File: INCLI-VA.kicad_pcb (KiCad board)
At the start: 2 copper layers, 100 x 70 mm, 186 parts, among them J1 MSTBV 2,5/5-GF-5,08, J2 MSTBV 2,5/2-GF-5,08, J401 USB4105-GF-A, J402 UART0, Q101 STD18NF25, Q102 IPD30N10S3L-34, Q701 DMN10H220LQ, Q702 BC817-40, Q703 BC807-40, Q751 DMN10H220LQ, Q752 BC817-40, Q753 BC807-40, SW401 RESET, SW402 BOOT, U101 LM74930QRGERQ1, U201 LMR38010SQDDARQ1, U301 TPS62A02QDRLRQ1, U302 LP5907QMFX-3.3Q1, U401 ESP32-S3-WROOM-1-N8R2, U402 USBLC6-2SC6, U501 SCL3300-D01, U502 ASM330LHHTR, U503 AS5147U-HTSM, U601 ADM3055E, U701 74AHCT1G126, U751 74AHCT1G126, U801 TPS3828-33Q1

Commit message: [Claude Code] PCB: adopta la propuesta 100x100 como INCLI-VA.kicad_pcb
Copia docs/layout/INCLI-VA-100x100.kicad_pcb sobre el PCB principal (sin
cambios propios desde 17a9676) y borra la copia duplicada de docs/layout.
DRC: 0 errores, 1 aviso U401, 396 sin rutear. Paridad: 22 diferencias por el
latch retirado; Update PCB from Schematic pendiente.

Co-Authored-By: Claude Opus 5.5 <noreply@anthropic.com>
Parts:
- removed H5: MountingHole_M3, MountingHole:MountingHole_3.2mm_M3
- TP101, TP102, TP103, TP104, TP201, TP301, TP302, TP303, TP304, TP305, TP501, TP502, TP503, TP504: moved to B.Cu
- moved H3 165.1 mm to (105.0, 145.0)
- moved SW401 163.0 mm to (181.0, 55.0)
- moved D601 152.8 mm to (116.0, 104.0)
- moved R754 151.9 mm to (195.0, 81.0), turned to 0 degrees
- moved R301 150.0 mm to (161.0, 118.0), turned to 0 degrees
- moved R752 149.7 mm to (190.5, 81.0)
- moved D752 149.5 mm to (193.5, 72.5), turned to 0 degrees
- moved C302 146.0 mm to (147.0, 120.0), turned to 0 degrees
- moved R755 145.9 mm to (196.0, 77.5), turned to 90 degrees
- moved R756 145.2 mm to (191.0, 84.0)
- moved SW402 145.0 mm to (186.0, 89.0)
- moved TP305 144.9 mm to (158.5, 138.5), turned to 180 degrees
- moved R108 144.5 mm to (115.0, 64.0)
- moved R112 144.5 mm to (144.0, 53.0)
- moved R603 144.2 mm to (116.0, 111.0)
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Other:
- board size 100 x 70 mm -> 100 x 100 mm

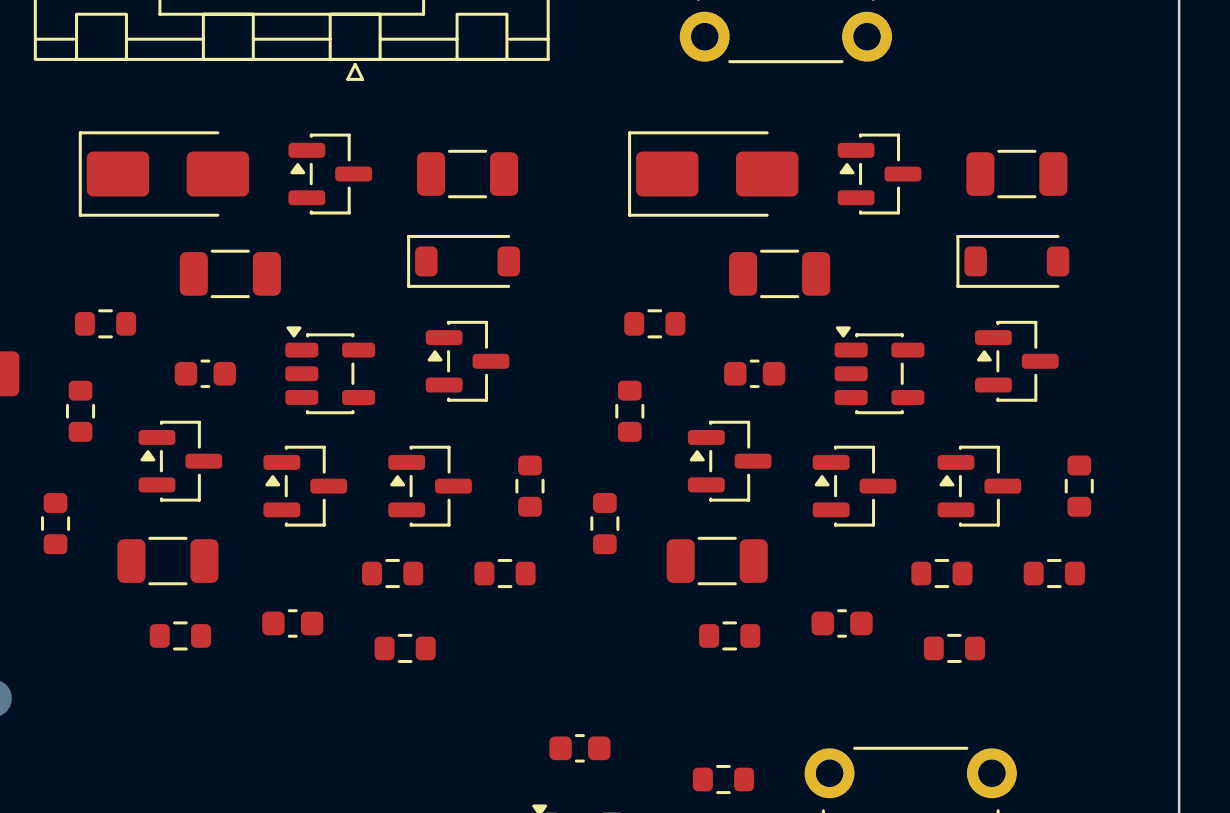
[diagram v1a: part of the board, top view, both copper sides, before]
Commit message: PCB: Update PCB from Schematic tras retirar el latch de DO (hecho por el usuario en KiCad, F8)
Quita las 18 huellas del latch (Q702/Q703/D702/R704-R707/C701/R701 y 75x) y
une la fuente de Q701/Q751 a GND_VEH. Paridad con el esquematico: 0.

Co-Authored-By: Claude Opus 5.5 <noreply@anthropic.com>
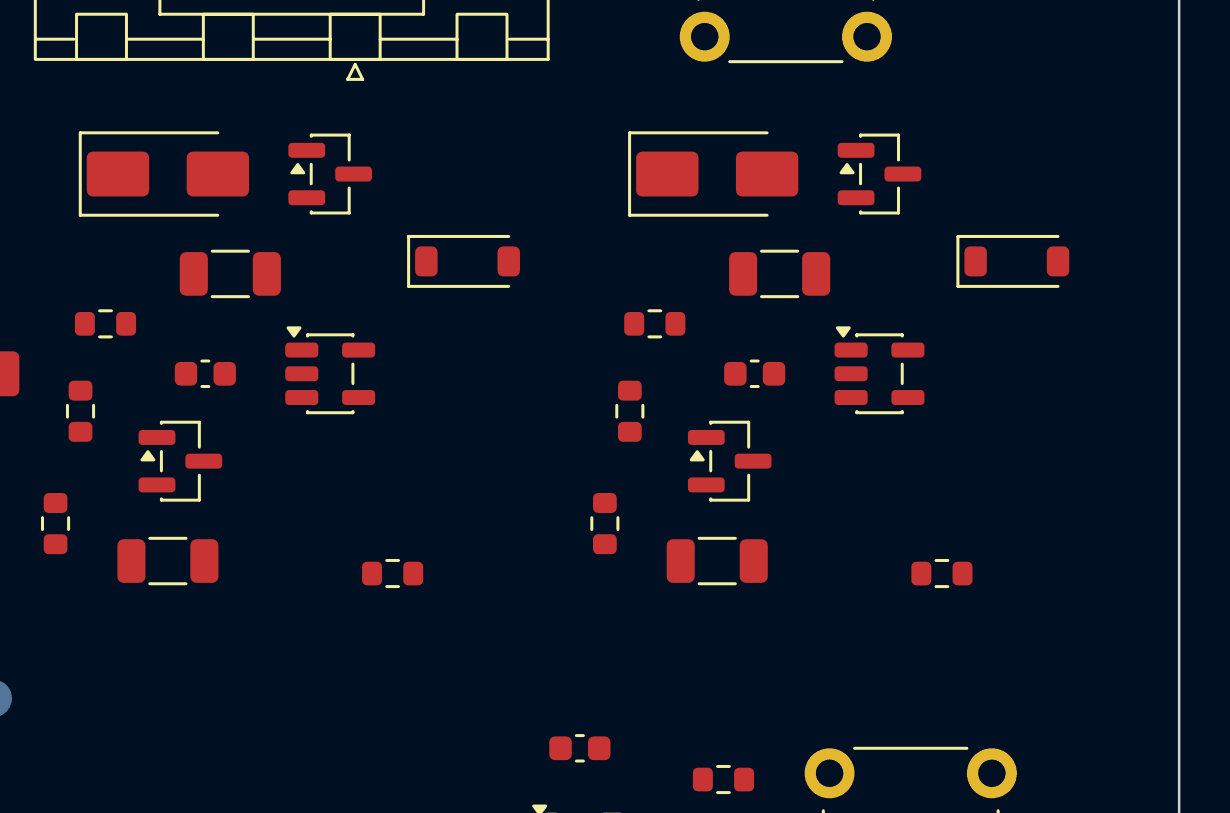
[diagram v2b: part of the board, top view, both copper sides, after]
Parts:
- removed C701, C751: 1nF, Capacitor_SMD:C_0603_1608Metric
- removed D702, D752: BAT54A, Package_TO_SOT_SMD:SOT-23
- removed Q702, Q752: BC817-40, Package_TO_SOT_SMD:SOT-23
- removed Q703, Q753: BC807-40, Package_TO_SOT_SMD:SOT-23
- removed R701, R751: 1R, Resistor_SMD:R_1206_3216Metric
- removed R704, R754: 47k, Resistor_SMD:R_0603_1608Metric
- removed R705, R707, R755, R757: 10k, Resistor_SMD:R_0603_1608Metric
- removed R706, R756: 1k, Resistor_SMD:R_0603_1608Metric
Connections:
- Q701 pad 2: /70_output_DO1/SENSE -> GND_VEH
- Q751 pad 2: /70_output_DO2/SENSE -> GND_VEH
